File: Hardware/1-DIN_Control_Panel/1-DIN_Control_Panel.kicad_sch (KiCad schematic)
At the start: 54 parts, among them J1 2x05 Molex Micro-Fit 3.0 43045, J2 Pot/SW - Brightness, J3 SW - Aux Jump-Start, J4 SW - Battery Bypass, J5 SW - Master Power, J6 Mode Controller, K1 FINDER-40.52, U1 LTV-847S, U10 CA56-12SEKWA, U2 LTV-847S, U3 MAX 6954 - SSOP, U4 12V->5V Variable Boost Buck C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, U8 LM324DR

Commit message: Added to schematic
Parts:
- removed J6: Mode Controller, Connector_Molex:Molex_Micro-Fit_3.0_43045-0812_2x04_P3.00mm_Vertical, symbol Connector:8P8C_Shielded
- added C11, C13, C14, C16, C17: 100nF, Capacitor_SMD:C_0603_1608Metric_Pad1.08x0.95mm_HandSolder, symbol Device:C
- added C12, C18: 22pF, Capacitor_SMD:C_0603_1608Metric_Pad1.08x0.95mm_HandSolder, symbol Device:C
- added C15: 47µF, Capacitor_SMD:C_0603_1608Metric_Pad1.08x0.95mm_HandSolder, symbol Device:C_Polarized
- added J6: Selector Knob Connector, libraries:Mystery_RJ45, symbol Connector:RJ32_Shielded
- added J7: UART Expansion, Connector_Molex:Molex_Micro-Fit_3.0_43045-0212_2x01_P3.00mm_Vertical, symbol Connector_Generic:Conn_01x02
- added R2, R20: 56kΩ, Resistor_SMD:R_0603_1608Metric_Pad0.98x0.95mm_HandSolder, symbol Device:R_US
- added R3: 10kΩ, Resistor_SMD:R_0603_1608Metric_Pad0.98x0.95mm_HandSolder, symbol Device:R_US
- added TP1, TP10, TP11, TP12, TP13, TP14, TP2, TP3, TP4, TP5, TP6, TP7, TP8, TP9: TestPoint_Flag, symbol Connector:TestPoint_Flag
- added U5: CA56-12SEKWA, Display_7Segment:CA56-12SEKWA, symbol Panel_Parts:COM-21212
- added U6: MAX 6954 - SSOP, symbol Panel_Parts:MAX_6954-SSOP
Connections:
- net +5V: now also J2.1 (A); no longer J2.2 (Wiper)
- net Arduino_MISO: now also U6.4 (DOUT)
- net Arduino_MOSI: now also U6.6 (DIN)
- net Arduino_SCK: now also U6.5 (CLK)
- net CURRENT_SENSE: now also C13.1; no longer C9.1
- net GND: now also C7.2, C8.2, J2.5 (Common), U3.16 (GND), U3.18 (GND), C11.2, C12.2, C13.2, C14.2, C15.2, C16.2, C17.2, C18.2, J6.SH, R2.1, R20.1, R3.1, U6.16 (GND), U6.18 (GND); no longer J2.4 (Open)
- net MODE_1: now also J?.1 (Pin_1), U2.1; no longer U2.2
- net MODE_12V: now also J?.8 (Pin_8), U1.8; no longer U1.7
- net MODE_1_LED: now also D4.1 (K), U2.16; no longer R13.1
- net MODE_2: now also J?.2 (Pin_2), U2.3; no longer U2.4
- net MODE_2_LED: now also D5.1 (K), U2.14; no longer R14.1
- net MODE_3: now also J?.3 (Pin_3), U2.5; no longer U2.6
- net MODE_3_LED: now also D6.1 (K), U2.12; no longer R15.1
- net MODE_4: now also J?.4 (Pin_4), U2.7; no longer U2.8
- net MODE_4_LED: now also D7.1 (K), U2.10; no longer R16.1
- net MODE_5: now also J?.5 (Pin_5), U1.1; no longer U1.2
- net MODE_5_LED: now also D8.1 (K), U1.16; no longer R17.1
- net MODE_6: now also J?.6 (Pin_6), U1.3; no longer U1.4
- net MODE_6_LED: now also D9.1 (K), U1.14; no longer R18.1
- net MODE_7: now also J?.7 (Pin_7), U1.5; no longer U1.6
- net MODE_7_LED: now also D10.1 (K), U1.12; no longer R19.1
- net MODE_PWR_DETECT: now also A1.7 (D4)
- net VOLTAGE_SENSE: now also A1.20 (A1), C9.1; no longer A1.19 (A0)
- net TX-EXPANSION: now reaches A1.1 (D1/TX)
- net TX-EXPANSION: now also J7.2 (Pin_2)
- net Arduino_~{CS}_VOLT: now reaches A1.12 (D9)
- net Arduino_~{CS}_VOLT: now also U3.3 (~{CS})
- net RX-EXPANSION: now reaches A1.2 (D0/RX)
- net RX-EXPANSION: now also J7.1 (Pin_1)
- net MODE_LED_BRIGHTNESS: now reaches A1.6 (D3)
- net MODE_LED_BRIGHTNESS: now also R13.1, R14.1, R15.1, R16.1, R17.1, R18.1, R19.1
- net VOLT_SOURCE_SELECT: now reaches D3.2 (A), K1.A2
- net VOLT_SOURCE_SELECT: now also J2.4 (Open); no longer J2.5 (Common)
- net at C7.1: now also C8.1, U3.19 (V+), U3.21 (V+), C11.1
- net DIGIT1_G2-N_ANODE: now reaches U10.1 (DIG1_G2-N_Anode)
- net DIGIT1_G2-N_ANODE: now also U3.8 (O1), U5.1 (DIG1_G2-N_Anode), U6.8 (O1)
- net DIGIT3_G2-N_ANODE: now reaches U10.10 (DIG3_G2-N_Anode)
- net DIGIT3_G2-N_ANODE: now also U3.12 (O5), U5.10 (DIG3_G2-N_Anode), U6.12 (O5)
- net DIGIT3_A-G1_ANODE: now reaches U10.11 (DIG3_A-G1_Anode)
- net DIGIT3_A-G1_ANODE: now also U3.11 (O4), U5.11 (DIG3_A-G1_Anode), U6.11 (O4)
- net F_CATHODE: now reaches U10.12 (F_Cathode)
- net F_CATHODE: now also U3.30 (O17), U5.12 (F_Cathode), U6.30 (O17)
- net B_CATHODE: now reaches U10.13 (B_Cathode)
- net B_CATHODE: now also U3.26 (O13), U5.13 (B_Cathode), U6.26 (O13)
- net A_CATHODE: now reaches U10.14 (A_Cathode)
- net A_CATHODE: now also U3.25 (O12), U5.14 (A_Cathode), U6.25 (O12)
- net DIGIT2_A-G1_ANODE: now reaches U10.15 (DIG2_A-G1_Anode)
- net DIGIT2_A-G1_ANODE: now also U3.9 (O2), U5.15 (DIG2_A-G1_Anode), U6.9 (O2)
- net DIGIT1_A-G1_ANODE: now reaches U10.16 (DIG1_A-G1_Anode)
- net DIGIT1_A-G1_ANODE: now also U3.7 (O0), U5.16 (DIG1_A-G1_Anode), U6.7 (O0)
- net DIGIT2_G2-N_ANODE: now reaches U10.2 (DIG2_G2-N_Anode)
- net DIGIT2_G2-N_ANODE: now also U3.10 (O3), U5.2 (DIG2_G2-N_Anode), U6.10 (O3)
- net D_CATHODE: now reaches U10.3 (D_Cathode)
- net D_CATHODE: now also U3.28 (O15), U5.3 (D_Cathode), U6.28 (O15)
- net C_CATHODE: now reaches U10.4 (C_Cathode)
- net C_CATHODE: now also U3.27 (O14), U5.4 (C_Cathode), U6.27 (O14)
- net G_CATHODE: now reaches U10.5 (G_Cathode)
- net G_CATHODE: now also U3.31 (O18), U5.5 (G_Cathode), U6.31 (O18)
- net E_CATHODE: now reaches U10.6 (E_Cathode)
- net E_CATHODE: now also U3.29 (O16), U5.6 (E_Cathode), U6.29 (O16)
- net COLON_DP_ANODE: now reaches U10.7 (COLON_DP_Anode)
- net COLON_DP_ANODE: now also U3.15 (O8), U5.7 (COLON_DP_Anode), U6.15 (O8)
- net DIGIT4_A-G1_ANODE: now reaches U10.8 (DIG4_A-G1_Anode)
- net DIGIT4_A-G1_ANODE: now also U3.13 (O6), U5.8 (DIG4_A-G1_Anode), U6.13 (O6)
- net DIGIT4_G2-N_ANODE: now reaches U10.9 (DIG4_G2-N_Anode)
- net DIGIT4_G2-N_ANODE: now also U3.14 (O7), U5.9 (DIG4_G2-N_Anode), U6.14 (O7)
- net at U3.1 (P0): now also TP3.1
- net at U3.17 (ISET): now also R2.2
- net at U3.2 (P1): now also TP4.1
- net at U3.20 (OSC): now also C12.1
- net at U3.32 (BLINK): now also TP1.1
- net at U3.33 (OSC_OUT): now also TP2.1
- net at U3.34 (P2): now also TP5.1
- net at U3.35 (P3): now also TP6.1
- net at U3.36 (P4): now also TP7.1
- net at J2.3 (B): now also R3.2
- net Arduino_~{CS} renamed Arduino_~{CS}_AMP
- net Arduino_~{CS}_AMP: now also U6.3 (~{CS}); no longer U3.3 (~{CS})
- new net: R20.2, U6.17 (ISET)
- new net: C15.1, C16.1, C17.1, U6.19 (V+), U6.21 (V+)
- new net: TP8.1, U6.1 (P0)
- new net: TP9.1, U6.2 (P1)
- new net: C18.1, U6.20 (OSC)
- new net: TP13.1, U6.32 (BLINK)
- new net: TP14.1, U6.33 (OSC_OUT)
- new net: TP10.1, U6.34 (P2)
- new net: TP11.1, U6.35 (P3)
- new net: TP12.1, U6.36 (P4)
- new net BRIGHTNESS_CONTROL: A1.19 (A0), C14.1, J2.2 (Wiper)
- new net MODE_12V_OUT: J6.8, U1.7
- new net MODE_1_OUT: J6.1, U2.2
- new net MODE_2_OUT: J6.2, U2.4
- new net MODE_3_OUT: J6.3, U2.6
- new net MODE_4_OUT: J6.4, U2.8
- new net MODE_5_OUT: J6.5, U1.2
- new net MODE_6_OUT: J6.6, U1.4
- new net MODE_7_OUT: J6.7, U1.6
- no-connect marks 5 -> 25
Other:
- note added: "14-Segment Ammeter Display & LED Driver"
- note added: "14-Segment Voltmeter Display & LED Driver"
- note added: "Arduino Header & Brightness Knob"
- note added: "Instrumentation Amplifier For Current Measurement"
- note added: "Main Input & Toggle Switches"
- note added: "Power Sourcing"
- note added: "Under normal operating conditions, this panel will follow the state of "MASTER". This relay allows the panel to be powered directly by the car's 12V battery, bypassing MASTER, enabling voltage measurements of the 12V battery when the ignition is set to OFF."
- moved on the sheet: C1, C10, C2, C3, C4, C5, C6, C7, C8, D1, D10, D2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

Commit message: Added footprints and sectioned the schematic
Still need to make sub pages and make a footprint for the MAX chips
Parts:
- removed C18: 22pF, Capacitor_SMD:C_0603_1608Metric_Pad1.08x0.95mm_HandSolder, symbol Device:C
- removed R20: 56kΩ, Resistor_SMD:R_0603_1608Metric_Pad0.98x0.95mm_HandSolder, symbol Device:R_US
- added C8: 22pF, Capacitor_SMD:C_0603_1608Metric_Pad1.08x0.95mm_HandSolder, symbol Device:C
- added R10: 56kΩ, Resistor_SMD:R_0603_1608Metric_Pad0.98x0.95mm_HandSolder, symbol Device:R_US
- D1: renamed from D4; footprint (none) -> LED_THT:LED_D3.0mm
- D2: renamed from D5; footprint (none) -> LED_THT:LED_D3.0mm
- D3: renamed from D6; footprint (none) -> LED_THT:LED_D3.0mm
- D4: renamed from D7; footprint (none) -> LED_THT:LED_D3.0mm
- D5: renamed from D8; footprint (none) -> LED_THT:LED_D3.0mm
- D6: renamed from D9; footprint (none) -> LED_THT:LED_D3.0mm
- D7: renamed from D10; footprint (none) -> LED_THT:LED_D3.0mm
- TP1: renamed from TP3; footprint (none) -> TestPoint:TestPoint_Loop_D2.54mm_Drill1.5mm_Beaded
- TP10, TP11, TP12, TP13, TP14, TP8, TP9: footprint (none) -> TestPoint:TestPoint_Loop_D2.54mm_Drill1.5mm_Beaded
- TP2: renamed from TP4; footprint (none) -> TestPoint:TestPoint_Loop_D2.54mm_Drill1.5mm_Beaded
- TP3: renamed from TP5; footprint (none) -> TestPoint:TestPoint_Loop_D2.54mm_Drill1.5mm_Beaded
- TP4: renamed from TP6; footprint (none) -> TestPoint:TestPoint_Loop_D2.54mm_Drill1.5mm_Beaded
- TP5: renamed from TP7; footprint (none) -> TestPoint:TestPoint_Loop_D2.54mm_Drill1.5mm_Beaded
- TP6: renamed from TP1; footprint (none) -> TestPoint:TestPoint_Loop_D2.54mm_Drill1.5mm_Beaded
- TP7: renamed from TP2; footprint (none) -> TestPoint:TestPoint_Loop_D2.54mm_Drill1.5mm_Beaded
- U5: renamed from U3; footprint (none) -> Package_SO:SSOP-44_5.3x12.8mm_P0.5mm
- U6: footprint (none) -> Package_SO:SSOP-44_5.3x12.8mm_P0.5mm
- gave numbers to parts that had none: 1
- renumbered C7 to C1, C14 to C10, C13 to C11, C4 to C12, C2 to C13, C3 to C14, C1 to C15, C5 to C16, C6 to C17, C10 to C18, C15 to C2, C8 to C3, C16 to C4, C11 to C5, C17 to C6, C12 to C7, D3 to D10, D1 to D8, D2 to D9, J6 to J1, J1 to J3, J7 to J4, J3 to J5, J4 to J6, J5 to J7, J2 to J8, R3 to R11, R4 to R12, R5 to R13, R6 to R14, R7 to R15, R8 to R16, R9 to R17, R10 to R18, R11 to R19, R13 to R2, R12 to R20, R14 to R3, R15 to R4, R16 to R5, R17 to R6, R18 to R7, R19 to R8, R2 to R9, U10 to U1, U5 to U2, U2 to U3, U1 to U4, U8 to U7, U4 to U8
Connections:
- net GND: now also C8.2, R10.1
- net at U6.17 (ISET): now also R10.2
- net at U6.20 (OSC): now also C8.1
- net at TP14.1, U6.33 (OSC_OUT): now also TP7.1, U5.33 (OSC_OUT)
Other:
- note added: "Mode Selector Knob"
- company: (none) -> KX0STL
- title: (none) -> 1-DIN Control Panel
- moved on the sheet: C7, R9

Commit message: Scooted some stuffs
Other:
- note added: "Mode Selector LED's PWM Brightness Control"
- note removed: "Mode Selector LED PWM Brightness Control"
- moved on the sheet: A1, C10, C11, C12, C9, J4, J8, R11, R12, R13

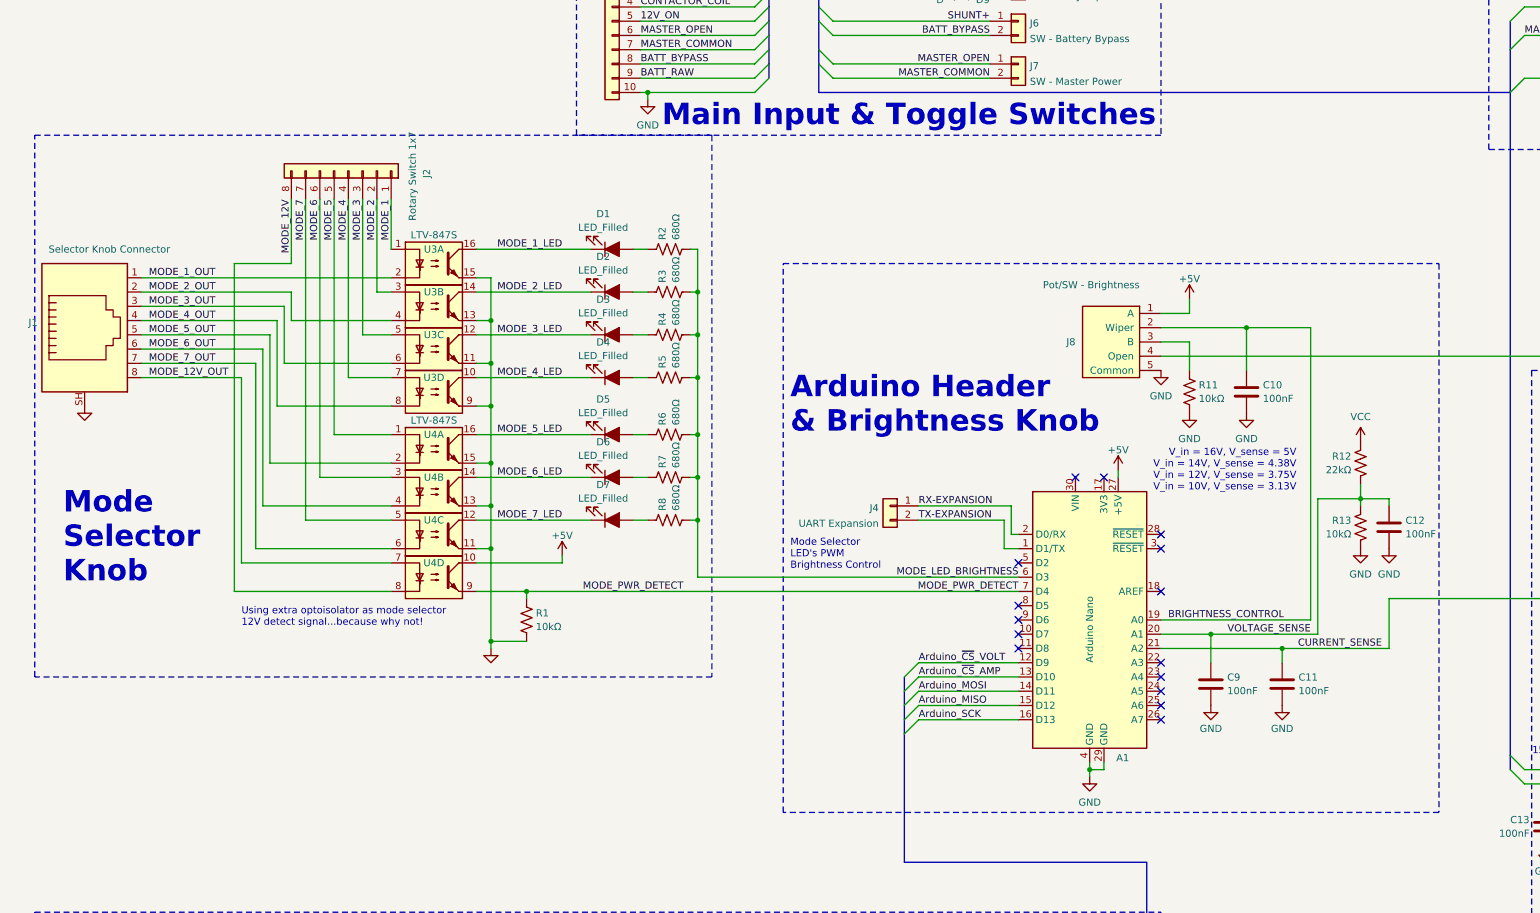
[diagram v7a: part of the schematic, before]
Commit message: Adjusted mode LEDs
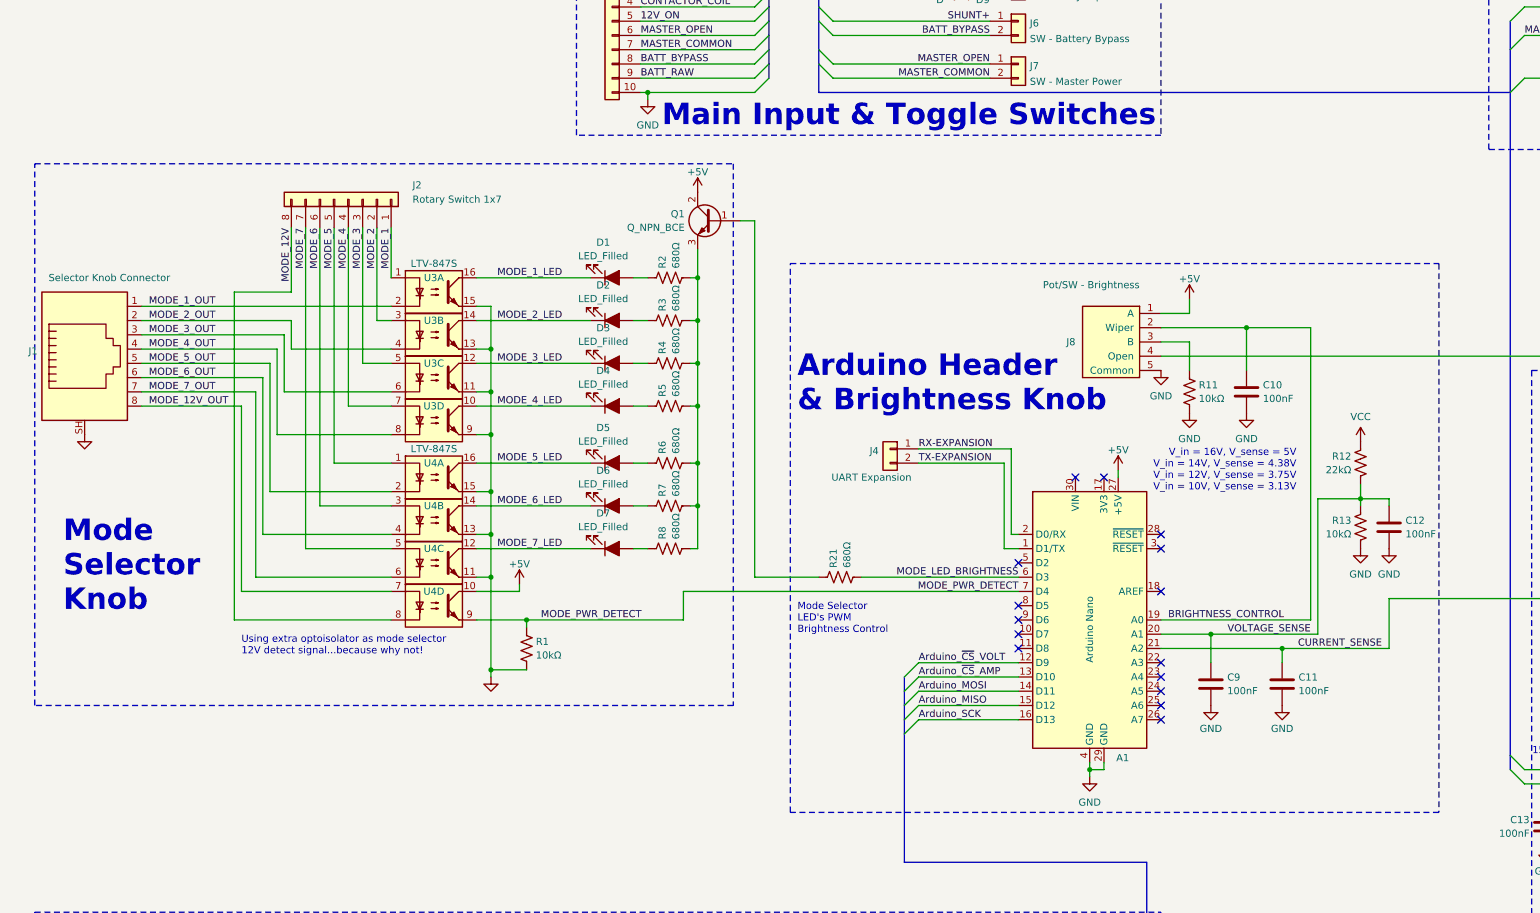
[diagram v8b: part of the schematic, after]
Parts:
- added Q1: Q_NPN_BCE, symbol Device:Q_NPN_BCE
- added R21: 680Ω, Resistor_SMD:R_0603_1608Metric_Pad0.98x0.95mm_HandSolder, symbol Device:R_US
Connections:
- net +5V: now also Q1.2 (C)
- net MODE_LED_BRIGHTNESS: now also R21.1; no longer R2.1, R3.1, R4.1, R5.1, R6.1, R7.1, R8.1
- new net: Q1.3 (E), R2.1, R3.1, R4.1, R5.1, R6.1, R7.1, R8.1
- new net: Q1.1 (B), R21.2
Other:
- moved on the sheet: D1, D2, D3, D4, D5, D6, D7, J1, J2, J4, R1, R2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
